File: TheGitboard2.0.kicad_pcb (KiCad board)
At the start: 2 copper layers, 78.3 x 70.1 mm, 9 parts, among them SW1 SW_Push, SW2 SW_Push, SW3 SW_Push, SW4 SW_Push, SW5 SW_Push, SW6 SW_Push, SW7 SW_Push, SW8 SW_Push, U1 MOUDLE-SEEEDUINO-XIAO

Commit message: PCB Save: 12 files changed TheGitboard2.0-B_Cu.gbl 2075/0/0 TheGitboard2.0-B_Mask.gbs 2115/0/0 TheGitboard2.0-B_Paste.gbp 1946/0/0 TheGitboard2.0-B_Silkscreen.gbo 2391/0/0 TheGitboard2.0-Edge_Cuts.gm1 1993/0/0 TheGitboard2.0-F_Cu.gtl 2211/0/0 TheGitboard2.0-F_Mask.gts 2057/0/0 TheGitboard2.0-F_Paste.gtp 1966/0/0 TheGitboard2.0-F_Silkscreen.gto 2487/0/0 TheGitboard2.0-job.gbrjob 125/0/0 TheGitboard2.0.kicad_pcb 111/0/150 ~TheGitboard2.0.kicad_pcb.lck 1/0/0
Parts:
- moved U1 6.69 mm to (157.6, 86.0)
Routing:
- net Net-(U1-PA6_A10_D10_MOSI): track 115.5 -> 188.2 mm
- net Net-(U1-GND): track 125.6 -> 190.2 mm
- net Net-(U1-PA7_A8_D8_SCK): track 85.6 -> 113.7 mm
- net Net-(U1-PA5_A9_D9_MISO): track 56.8 -> 68.5 mm
- net Net-(U1-3V3): track 85.3 -> 96.6 mm

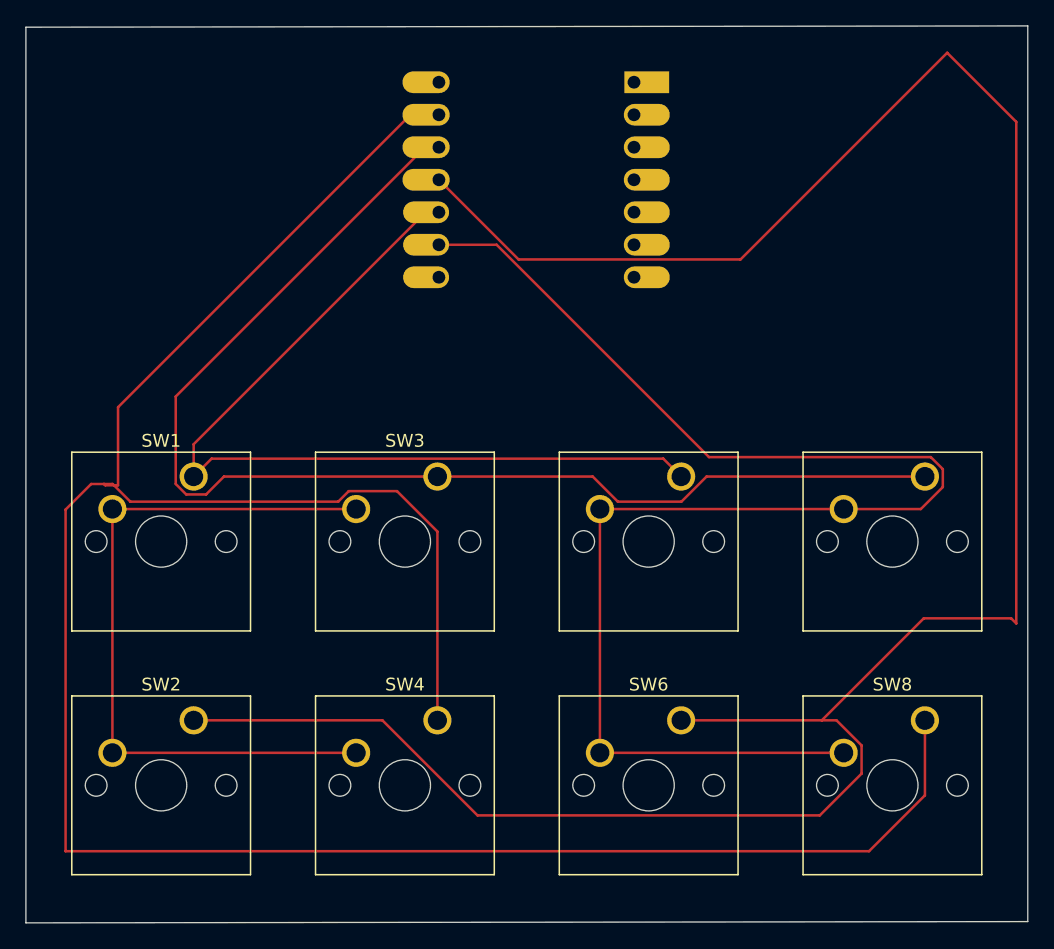
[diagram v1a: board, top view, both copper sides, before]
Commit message: PCB Save: 2 files changed TheGitboard2.0.kicad_pcb 0/510/18 TheGitboard2.0.kicad_prl 0/0/1
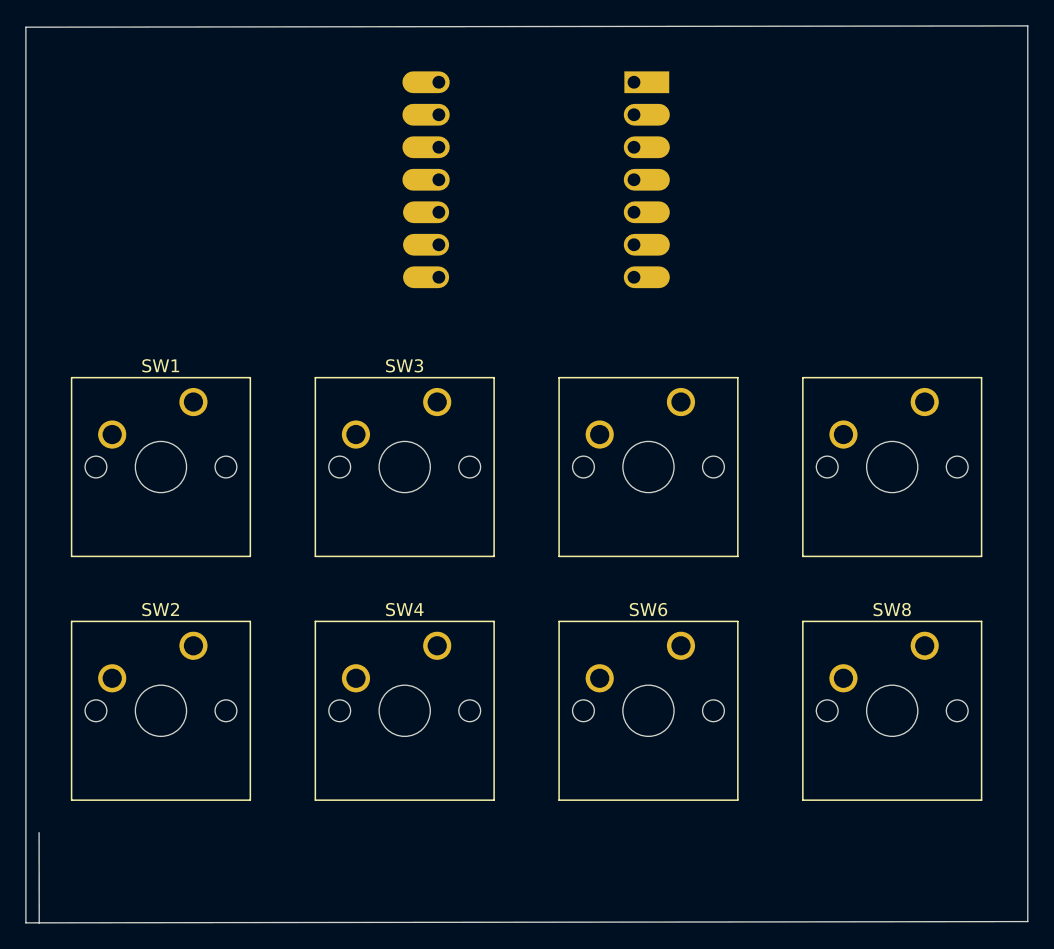
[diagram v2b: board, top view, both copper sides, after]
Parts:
- moved SW2 5.83 mm to (130.8, 122.4)
- moved SW4 5.83 mm to (149.8, 122.4)
- moved SW6 5.83 mm to (168.9, 122.4)
- moved SW8 5.83 mm to (187.9, 122.4)
- moved SW1 5.83 mm to (130.8, 103.4)
- moved SW3 5.83 mm to (149.8, 103.4)
- moved SW5 5.83 mm to (168.9, 103.4)
- moved SW7 5.83 mm to (187.9, 103.4)
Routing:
- net Net-(U1-GND): track 190.2 -> 0.00 mm
- net Net-(U1-PA6_A10_D10_MOSI): track 188.2 -> 0.00 mm
- net Net-(U1-PA7_A8_D8_SCK): track 113.7 -> 0.00 mm
- net Net-(U1-3V3): track 96.6 -> 0.00 mm
- net Net-(U1-PA5_A9_D9_MISO): track 68.5 -> 0.00 mm
- net Net-(SW1-Pad2): track 57.1 -> 0.00 mm
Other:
- outline, holes or cut-outs redrawn

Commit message: Autosave
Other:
- outline, holes or cut-outs redrawn
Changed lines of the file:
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@@
-	)
-	(gr_line
-		(start 118.74 144.12)
-		(end 118.73 137.05)
-		(stroke
-			(width 0.05)
-			(type default)
-		)
-		(layer "Edge.Cuts")
 	)
 	(gr_line

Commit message: Autosave
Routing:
- net Net-(U1-PA7_A8_D8_SCK): track 0.00 -> 57.2 mm
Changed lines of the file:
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@@
 		(layer "Edge.Cuts")
+	)
+	(segment
+		(start 181.595 105.935)
+		(end 162.545 105.935)
+		(width 0.2)
+		(layer "F.Cu")
+		(net "Net-(U1-PA7_A8_D8_SCK)")
+	)
+	(segment
+		(start 162.545 105.935)
+		(end 162.545 124.985)
+		(width 0.2)
+		(layer "F.Cu")
+		(net "Net-(U1-PA7_A8_D8_SCK)")
+	)
+	(segment
+		(start 181.595 124.985)
+		(end 162.545 124.985)
+		(width 0.2)
+		(layer "F.Cu")
+		(net "Net-(U1-PA7_A8_D8_SCK)")
 	)
 	(embedded_fonts no)

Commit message: Autosave
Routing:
- net Net-(U1-PA7_A8_D8_SCK): track 57.2 -> 78.9 mm
- net Net-(SW1-Pad2): track 0.00 -> 19.1 mm
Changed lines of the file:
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@@
+	)
+	(segment
+		(start 162.545 105.935)
+		(end 162.545 100.705)
+		(width 0.2)
+		(layer "F.Cu")
+		(net "Net-(U1-PA7_A8_D8_SCK)")
 	)
 	(segment
 		(start 181.595 105.935)
 		(end 162.545 105.935)
+		(width 0.2)
+		(layer "F.Cu")
+		(net "Net-(U1-PA7_A8_D8_SCK)")
+	)
+	(segment
+		(start 152.94403 91.10403)
+		(end 149.975 91.10403)
 		(width 0.2)
 		(layer "F.Cu")
@@
 		(net "Net-(U1-PA7_A8_D8_SCK)")
 	)
+	(segment
+		(start 162.545 100.705)
+		(end 152.94403 91.10403)
+		(width 0.2)
+		(layer "F.Cu")
+		(net "Net-(U1-PA7_A8_D8_SCK)")
+	)
+	(segment
+		(start 143.495 105.935)
+		(end 124.445 105.935)
+		(width 0.2)
+		(layer "F.Cu")
+		(net "Net-(SW1-Pad2)")
+	)
 	(embedded_fonts no)

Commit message: Autosave
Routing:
- net Net-(SW1-Pad2): track 19.1 -> 57.2 mm
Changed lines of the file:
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@@
+	)
+	(segment
+		(start 124.445 124.985)
+		(end 143.495 124.985)
+		(width 0.2)
+		(layer "F.Cu")
+		(net "Net-(SW1-Pad2)")
 	)
 	(segment
@@
 		(width 0.2)
 		(layer "F.Cu")
+		(net "Net-(SW1-Pad2)")
+	)
+	(segment
+		(start 124.445 105.935)
+		(end 124.445 124.985)
+		(width 0.2)
+		(layer "F.Cu")

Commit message: Autosave
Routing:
- net Net-(U1-PA6_A10_D10_MOSI): track 0.00 -> 101.8 mm
- net Net-(U1-GND): track 0.00 -> 44.3 mm
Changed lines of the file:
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@@
+	)
+	(segment
+		(start 193.28 127.52)
+		(end 193.28 122.85)
+		(width 0.2)
+		(layer "F.Cu")
+		(net "Net-(U1-PA6_A10_D10_MOSI)")
+	)
+	(segment
+		(start 185.02 135.78)
+		(end 193.28 127.52)
+		(width 0.2)
+		(layer "F.Cu")
+		(net "Net-(U1-PA6_A10_D10_MOSI)")
+	)
+	(segment
+		(start 130.795 122.445)
+		(end 145.548402 122.445)
+		(width 0.2)
+		(layer "F.Cu")
+		(net "Net-(U1-PA6_A10_D10_MOSI)")
+	)
+	(segment
+		(start 158.883402 135.78)
+		(end 185.02 135.78)
+		(width 0.2)
+		(layer "F.Cu")
+		(net "Net-(U1-PA6_A10_D10_MOSI)")
+	)
+	(segment
+		(start 193.28 122.85)
+		(end 191.475 121.045)
+		(width 0.2)
+		(layer "F.Cu")
+		(net "Net-(U1-PA6_A10_D10_MOSI)")
+	)
+	(segment
+		(start 145.548402 122.445)
+		(end 158.883402 135.78)
+		(width 0.2)
+		(layer "F.Cu")
+		(net "Net-(U1-PA6_A10_D10_MOSI)")
+	)
+	(segment
+		(start 191.475 121.045)
+		(end 170.295 121.045)
+		(width 0.2)
+		(layer "F.Cu")
+		(net "Net-(U1-PA6_A10_D10_MOSI)")
+	)
+	(segment
+		(start 170.295 121.045)
+		(end 168.895 122.445)
+		(width 0.2)
+		(layer "F.Cu")
+		(net "Net-(U1-PA6_A10_D10_MOSI)")
 	)
 	(segment
@@
 		(net "Net-(SW1-Pad2)")
 	)
+	(segment
+		(start 187.102056 122.445)
+		(end 179.672056 129.875)
+		(width 0.2)
+		(layer "F.Cu")
+		(net "Net-(U1-GND)")
+	)
+	(segment
+		(start 157.275 129.875)
+		(end 149.845 122.445)
+		(width 0.2)
+		(layer "F.Cu")
+		(net "Net-(U1-GND)")
+	)
+	(segment
+		(start 179.672056 129.875)
+		(end 157.275 129.875)
+		(width 0.2)
+		(layer "F.Cu")
+		(net "Net-(U1-GND)")
+	)
+	(segment
+		(start 187.945 122.445)
+		(end 187.102056 122.445)
+		(width 0.2)
+		(layer "F.Cu")
+		(net "Net-(U1-GND)")
+	)
 	(embedded_fonts no)

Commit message: Autosave
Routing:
- net Net-(U1-PA5_A9_D9_MISO): track 0.00 -> 50.4 mm
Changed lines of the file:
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@@
+	)
+	(segment
+		(start 168.895 103.395)
+		(end 154.06403 88.56403)
+		(width 0.2)
+		(layer "F.Cu")
+		(net "Net-(U1-PA5_A9_D9_MISO)")
+	)
+	(segment
+		(start 154.06403 88.56403)
+		(end 149.975 88.56403)
+		(width 0.2)
+		(layer "F.Cu")
+		(net "Net-(U1-PA5_A9_D9_MISO)")
+	)
+	(segment
+		(start 145.62597 88.56403)
+		(end 149.975 88.56403)
+		(width 0.2)
+		(layer "F.Cu")
+		(net "Net-(U1-PA5_A9_D9_MISO)")
+	)
+	(segment
+		(start 130.795 103.395)
+		(end 145.62597 88.56403)
+		(width 0.2)
+		(layer "F.Cu")
+		(net "Net-(U1-PA5_A9_D9_MISO)")
 	)
 	(segment
